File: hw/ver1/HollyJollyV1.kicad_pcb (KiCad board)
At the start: 4 copper layers, 68.5 x 85.6 mm, 84 parts, among them J1 USB_B_Micro, Q1 2N7002, SW1 BOOT, SW2 CYCLE, U1 RP2040, U2 W25Q128JVS, U3 XC6206PxxxMR, Y1 12MHz

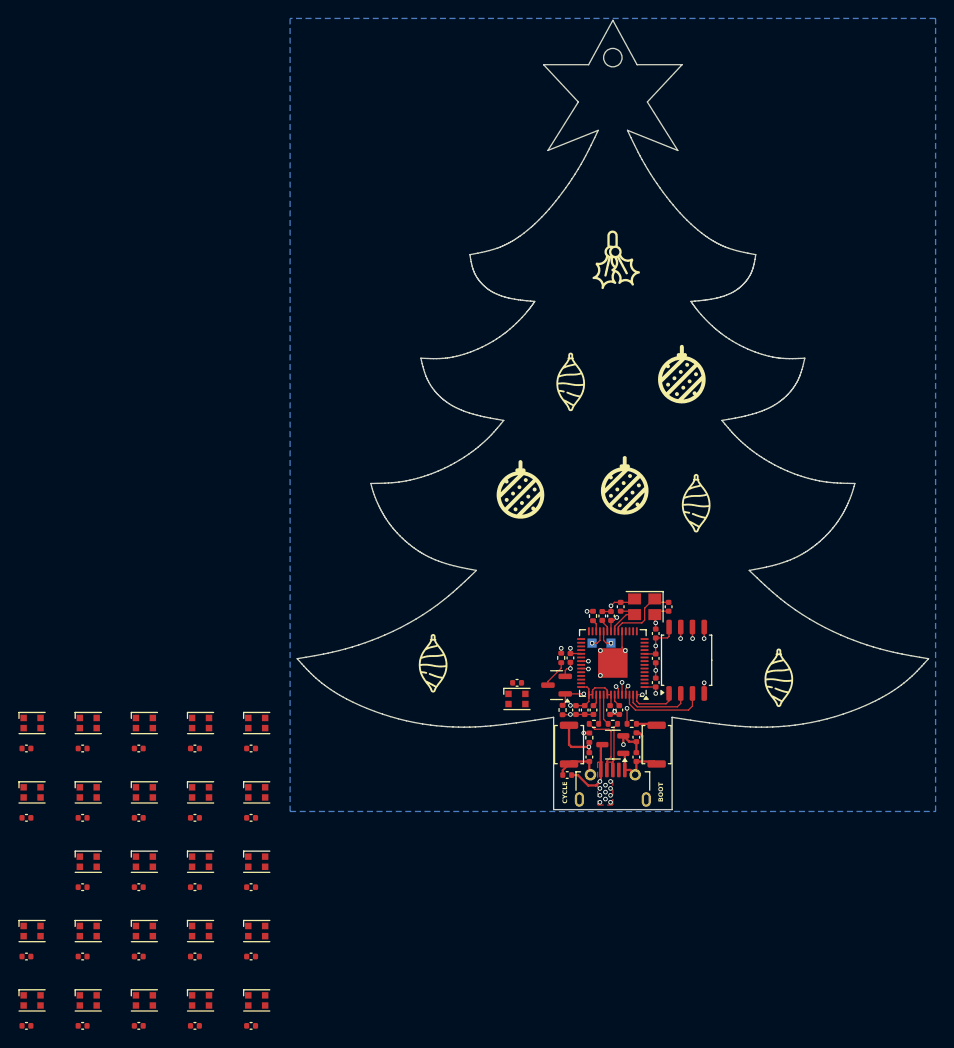
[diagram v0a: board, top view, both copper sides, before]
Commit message: Nearly have all the LEDs wired up. Improve the christmas cheer.
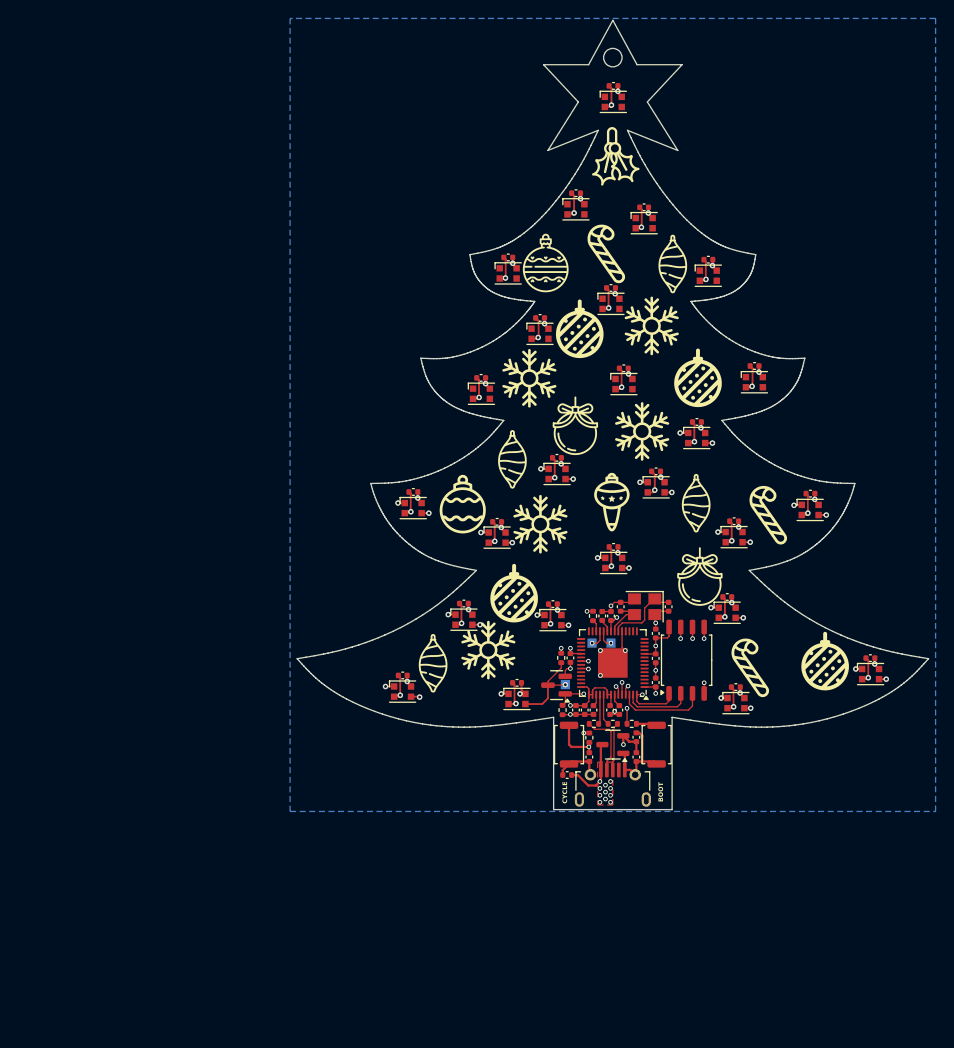
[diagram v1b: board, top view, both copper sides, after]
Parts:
- added TP3: LED_DATA_TP, TestPoint:TestPoint_Pad_1.0x1.0mm, B.Cu at (144.8, 129.2)
- moved C39 101.5 mm to (153.4, 77.5), turned to 180 degrees
- moved C38 100.0 mm to (160.4, 83.2), turned to 180 degrees
- moved C27 98.7 mm to (171.4, 108.5), turned to 180 degrees
- moved D22 97.6 mm to (153.4, 79.2)
- moved D21 96.0 mm to (160.3, 84.9)
- moved D10 95.9 mm to (171.4, 110.3)
- moved C25 93.1 mm to (177.9, 126.4), turned to 180 degrees
- moved D8 91.8 mm to (177.9, 128.1)
- moved C37 88.8 mm to (149.8, 86.2), turned to 180 degrees
- moved C42 88.6 mm to (150.1, 64.3), turned to 180 degrees
- moved C41 85.9 mm to (146.0, 76.0), turned to 180 degrees
- moved D20 84.8 mm to (149.8, 88.0)
- moved D25 84.3 mm to (150.1, 66.0)
- moved C22 82.2 mm to (150.1, 114.3), turned to 180 degrees
- moved D24 81.6 mm to (146.0, 77.7)
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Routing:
- net GND: track 35.3 -> 110.3 mm, vias 10 -> 35
- net +5V: track 8.36 -> 43.4 mm, vias 12 -> 37
- net /LED1/DOUT: track 0.00 -> 15.8 mm, vias 0 -> 2
- net /LED/DOUT: track 0.00 -> 10.7 mm, vias 0 -> 2
- net /LED_DOUT: track 3.04 -> 9.08 mm, vias 0 -> 1
- net /LED8/DOUT: track 0.00 -> 1.67 mm, vias 0 -> 2
- net /LED4/DOUT: track 0.00 -> 1.67 mm, vias 0 -> 2
- net /LED10/DIN: track 0.00 -> 1.64 mm, vias 0 -> 2
- net /LED13/DOUT: track 0.00 -> 1.62 mm, vias 0 -> 2
- net /LED11/DOUT: track 0.00 -> 1.62 mm, vias 0 -> 2
- net /LED2/DOUT: track 0.00 -> 1.57 mm, vias 0 -> 2
- net /LED10/DOUT: track 0.00 -> 1.57 mm, vias 0 -> 2
- net /LED12/DOUT: track 0.00 -> 1.57 mm, vias 0 -> 2
- net /LED7/DOUT: track 0.00 -> 1.52 mm, vias 0 -> 2
- net /LED5/DOUT: track 0.00 -> 1.52 mm, vias 0 -> 2
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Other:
- board text added: "DAT"

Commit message: Hardware version 1 complete and ordered.
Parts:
- added C43: 100nF, Capacitor_SMD:C_0402_1005Metric, F.Cu at (139.6, 127.8)
- added C44: 100nF, Capacitor_SMD:C_0402_1005Metric, F.Cu at (155.7, 113.3)
- added C45: 100nF, Capacitor_SMD:C_0402_1005Metric, F.Cu at (168.1, 123.9)
- added C46: 100nF, Capacitor_SMD:C_0402_1005Metric, F.Cu at (122.0, 126.5)
- added C47: 100nF, Capacitor_SMD:C_0402_1005Metric, F.Cu at (148.3, 64.7)
- added C48: 100nF, Capacitor_SMD:C_0402_1005Metric, F.Cu at (150.0, 63.5)
- added C49: 100nF, Capacitor_SMD:C_0402_1005Metric, F.Cu at (151.7, 64.7)
- added C50: 100nF, Capacitor_SMD:C_0402_1005Metric, F.Cu at (151.3, 66.5)
- added D26: WS2812B-2020, LED_SMD:LED_WS2812B-2020_PLCC4_2.0x2.0mm, F.Cu at (155.7, 115.0)
- added D27: WS2812B-2020, LED_SMD:LED_WS2812B-2020_PLCC4_2.0x2.0mm, F.Cu at (168.1, 125.7)
- added D28: WS2812B-2020, LED_SMD:LED_WS2812B-2020_PLCC4_2.0x2.0mm, F.Cu at (122.0, 128.2)
- added D29: WS2812B-2020, LED_SMD:LED_WS2812B-2020_PLCC4_2.0x2.0mm, F.Cu at (146.5, 63.8)
- added D30: WS2812B-2020, LED_SMD:LED_WS2812B-2020_PLCC4_2.0x2.0mm, F.Cu at (150.0, 61.5)
- added D31: WS2812B-2020, LED_SMD:LED_WS2812B-2020_PLCC4_2.0x2.0mm, F.Cu at (153.5, 63.8)
- added D32: WS2812B-2020, LED_SMD:LED_WS2812B-2020_PLCC4_2.0x2.0mm, F.Cu at (152.8, 67.8)
- added R8: 10k, Resistor_SMD:R_0402_1005Metric, F.Cu at (141.4, 127.8)
- added SW3: BRIGHT, Button_Switch_SMD:SW_Push_SPST_NO_Alps_SKRK, F.Cu at (141.1, 125.5)
- moved D2 5.04 mm to (131.9, 131.9)
- moved C19 5.04 mm to (131.9, 130.2)
- moved D25 3.39 mm to (147.2, 67.8), turned to 40 degrees
- moved C22 2.73 mm to (147.4, 114.2)
- moved D5 2.73 mm to (147.4, 115.9)
- moved C42 2.62 mm to (148.7, 66.5), turned to -50 degrees
- moved C2 0.65 mm to (145.4, 139.6), turned to 90 degrees
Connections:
- D3 pad 3: /LED1/DOUT -> /LED2/DIN
- D5 pad 1: /LED4/DOUT -> /LED25/DIN
- D6 pad 3: /LED4/DOUT -> /LED25/DOUT
- D8 pad 1: /LED7/DOUT -> /LED26/DIN
- D9 pad 3: /LED7/DOUT -> /LED26/DOUT
- U1 pad 30: unconnected-(U1-GPIO19-Pad30) -> /LED_BRIGHT
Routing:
- net /LED12/DOUT: track 1.57 -> 21.6 mm
- net /LED13/DOUT: track 1.62 -> 21.4 mm
- net /LED2/DIN: track 0.00 -> 19.2 mm, vias 0 -> 2
- net /LED6/DOUT: track 1.47 -> 20.3 mm
- net /LED10/DOUT: track 1.57 -> 18.1 mm
- net /LED19/DOUT: track 0.00 -> 16.0 mm, vias 0 -> 2
- net /LED21/DOUT: track 0.00 -> 15.7 mm, vias 0 -> 2
- net /LED25/DOUT: track 0.00 -> 15.2 mm, vias 0 -> 2
- net /LED5/DOUT: track 1.52 -> 16.7 mm
- net /LED22/DOUT: track 0.00 -> 14.7 mm, vias 0 -> 2
- net /LED16/DOUT: track 0.00 -> 14.5 mm, vias 0 -> 2
- net /LED26/DOUT: track 0.00 -> 14.1 mm, vias 0 -> 2
- net /LED10/DIN: track 1.64 -> 15.5 mm
- net /LED2/DOUT: track 1.57 -> 15.3 mm
- net /LED25/DIN: track 0.00 -> 13.7 mm, vias 0 -> 2
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- added copper zone on F.Cu, net GND
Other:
- outline, holes or cut-outs redrawn
- board text added: "Boot"
- board text added: "Bright"
- board text added: "Github: brandonbraun653/HollyJolly"
- board text added: "HW Ver: 1"
- board text added: "Holly"
- board text added: "Jolly"
- board text added: "Merry"
- board text added: "clk"
- board text added: "data"
- board text added: "swd"
- board text removed: "BOOT"
- board text removed: "CLK"
- board text removed: "CYCLE"
- board text removed: "DAT"
- board text removed: "SWD"
